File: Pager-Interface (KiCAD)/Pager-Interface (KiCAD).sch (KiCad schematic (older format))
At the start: 18 parts

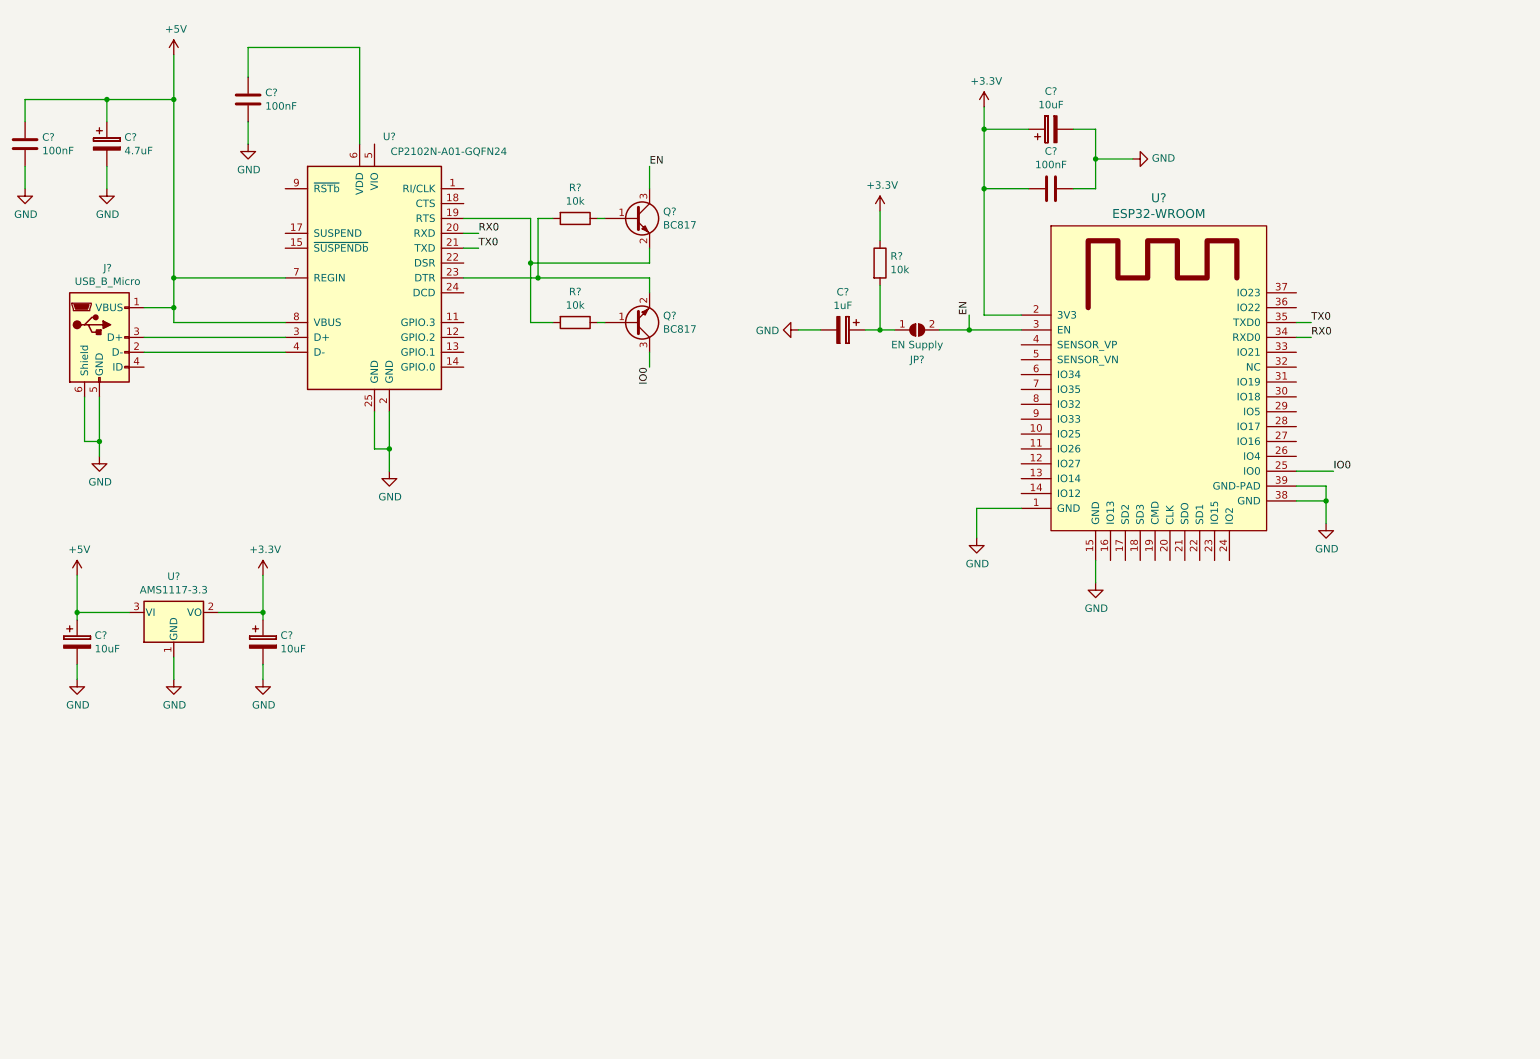
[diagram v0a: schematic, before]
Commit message: added si4432 symbol + added and connected si4432 in schematic
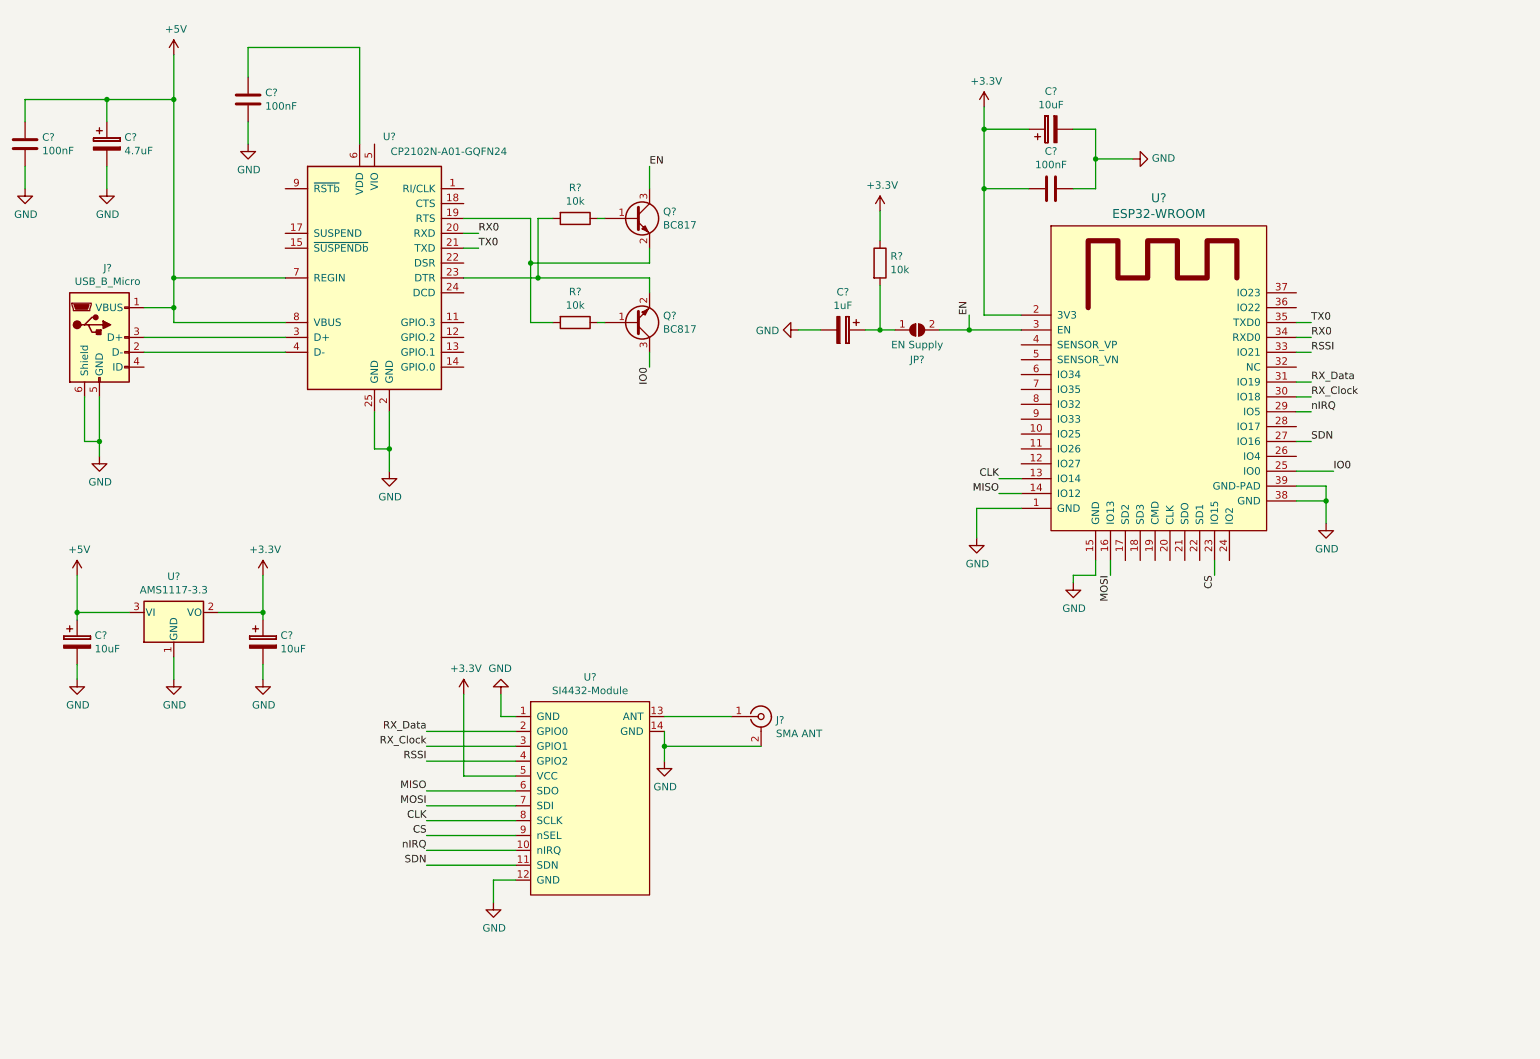
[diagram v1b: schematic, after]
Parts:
- added J?: SMA ANT, symbol Connector:Conn_Coaxial
- added U?: SI4432-Module, symbol si4432:SI4432-Module
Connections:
- net +3V3: now also U?.5 (VCC)
- net GND: now also J?.2 (Ext), U?.1 (GND), U?.12 (GND), U?.14 (GND)
- net CLK: now reaches U?.13 (IO14)
- net CLK: now also U?.8 (SCLK)
- net MISO: now reaches U?.14 (IO12)
- net MISO: now also U?.6 (SDO)
- net MOSI: now reaches U?.16 (IO13)
- net MOSI: now also U?.7 (SDI)
- net CS: now reaches U?.23 (IO15)
- net CS: now also U?.9 (nSEL)
- net SDN: now reaches U?.27 (IO16)
- net SDN: now also U?.11 (SDN)
- net nIRQ: now reaches U?.29 (IO5)
- net nIRQ: now also U?.10 (nIRQ)
- net RX_Clock: now reaches U?.30 (IO18)
- net RX_Clock: now also U?.3 (GPIO1)
- net RX_Data: now reaches U?.31 (IO19)
- net RX_Data: now also U?.2 (GPIO0)
- net RSSI: now reaches U?.33 (IO21)
- net RSSI: now also U?.4 (GPIO2)
- new net: J?.1 (In), U?.13 (ANT)
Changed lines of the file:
@@
 L power:GND #PWR?
 U 1 1 6037F357
-P 8150 4500
-F 0 "#PWR?" H 8150 4250 50  0001 C CNN
-F 1 "GND" H 8155 4327 50  0000 C CNN
-F 2 "" H 8150 4500 50  0001 C CNN
-F 3 "" H 8150 4500 50  0001 C CNN
-	1    8150 4500
-	1    0    0    -1
-$EndComp
-Wire Wire Line
-	8150 4350 8150 4500
+P 8000 4500
+F 0 "#PWR?" H 8000 4250 50  0001 C CNN
+F 1 "GND" H 8005 4327 50  0000 C CNN
+F 2 "" H 8000 4500 50  0001 C CNN
+F 3 "" H 8000 4500 50  0001 C CNN
+	1    8000 4500
+	1    0    0    -1
+$EndComp
 Wire Wire Line
 	9500 3850 9700 3850
@@
 	2550 4450 2550 4700
 Connection ~ 2550 4700
+$Comp
+L si4432:SI4432-Module U?
+U 1 1 6039ABF6
+P 4750 5900
+F 0 "U?" H 4750 6665 50  0000 C CNN
+F 1 "SI4432-Module" H 4750 6574 50  0000 C CNN
+F 2 "" H 5400 6450 50  0001 C CNN
+F 3 "" H 5400 6450 50  0001 C CNN
+	1    4750 5900
+	1    0    0    -1
+$EndComp
+$Comp
+L Connector:Conn_Coaxial J?
+U 1 1 6039ADF5
+P 5900 5400
+F 0 "J?" H 6000 5376 50  0000 L CNN
+F 1 "SMA ANT" H 6000 5285 50  0000 L CNN
+F 2 "" H 5900 5400 50  0001 C CNN
+F 3 " ~" H 5900 5400 50  0001 C CNN
+	1    5900 5400
+	1    0    0    -1
+$EndComp
+Wire Wire Line
+	5250 5400 5700 5400
+Wire Wire Line
+	5900 5600 5250 5600
+Wire Wire Line
+	5250 5600 5250 5500
+Wire Wire Line
+	4250 5400 4150 5400
+Wire Wire Line
+	4150 5400 4150 5250
+Wire Wire Line
+	4250 6500 4100 6500
+Wire Wire Line
+	4100 6500 4100 6650
+$Comp
+L power:GND #PWR?
+U 1 1 603A1EF6
+P 5250 5700
+F 0 "#PWR?" H 5250 5450 50  0001 C CNN
+F 1 "GND" H 5255 5527 50  0000 C CNN
+F 2 "" H 5250 5700 50  0001 C CNN
+F 3 "" H 5250 5700 50  0001 C CNN
+	1    5250 5700
+	1    0    0    -1
+$EndComp
+Wire Wire Line
+	5250 5600 5250 5700
+Connection ~ 5250 5600
+$Comp
+L power:GND #PWR?
+U 1 1 603A3E00
+P 4150 5250
+F 0 "#PWR?" H 4150 5000 50  0001 C CNN
+F 1 "GND" H 4155 5077 50  0000 C CNN
+F 2 "" H 4150 5250 50  0001 C CNN
+F 3 "" H 4150 5250 50  0001 C CNN
+	1    4150 5250
+	-1   0    0    1
+$EndComp
+$Comp
+L power:GND #PWR?
+U 1 1 603A3EA1
+P 4100 6650
+F 0 "#PWR?" H 4100 6400 50  0001 C CNN
+F 1 "GND" H 4105 6477 50  0000 C CNN
+F 2 "" H 4100 6650 50  0001 C CNN
+F 3 "" H 4100 6650 50  0001 C CNN
+	1    4100 6650
+	1    0    0    -1
+$EndComp
+Wire Wire Line
+	4250 5800 3900 5800
+Wire Wire Line
+	3900 5800 3900 5250
+$Comp
+L power:+3.3V #PWR?
+U 1 1 603A5FDC
+P 3900 5250
+F 0 "#PWR?" H 3900 5100 50  0001 C CNN
+F 1 "+3.3V" H 3915 5423 50  0000 C CNN
+F 2 "" H 3900 5250 50  0001 C CNN
+F 3 "" H 3900 5250 50  0001 C CNN
+	1    3900 5250
+	1    0    0    -1
+$EndComp
+Wire Wire Line
+	4250 5500 3650 5500
+Wire Wire Line
+	4250 5600 3650 5600
+Wire Wire Line
+	4250 5700 3650 5700
+Text Label 3650 5500 2    50   ~ 0
+RX_Data
+Text Label 3650 5600 2    50   ~ 0
+RX_Clock
+Text Label 3650 5700 2    50   ~ 0
+RSSI
+Wire Wire Line
+	4250 5900 3650 5900
+Wire Wire Line
+	4250 6000 3650 6000
+Wire Wire Line
+	4250 6100 3650 6100
+Wire Wire Line
+	4250 6200 3650 6200
+Text Label 3650 5900 2    50   ~ 0
+MISO
+Text Label 3650 6000 2    50   ~ 0
+MOSI
+Text Label 3650 6100 2    50   ~ 0
+CLK
+Text Label 3650 6200 2    50   ~ 0
+CS
+Wire Wire Line
+	4250 6300 3650 6300
+Wire Wire Line
+	4250 6400 3650 6400
+Text Label 3650 6300 2    50   ~ 0
+nIRQ
+Text Label 3650 6400 2    50   ~ 0
+SDN
+Text Label 9600 3250 0    50   ~ 0
+RX_Clock
+Wire Wire Line
+	9500 3250 9600 3250
+Text Label 9600 3150 0    50   ~ 0
+RX_Data
+Wire Wire Line
+	9500 3150 9600 3150
+Text Label 9600 2950 0    50   ~ 0
+RSSI
+Wire Wire Line
+	9500 2950 9600 2950
+Text Label 9600 3350 0    50   ~ 0
+nIRQ
+Wire Wire Line
+	9600 3350 9500 3350
+Text Label 9600 3550 0    50   ~ 0
+SDN
+Wire Wire Line
+	9500 3550 9600 3550
+Text Label 7500 3900 2    50   ~ 0
+MISO
+Wire Wire Line
+	7650 3900 7500 3900
+Text Label 8250 4450 3    50   ~ 0
+MOSI
+Wire Wire Line
+	8150 4350 8150 4450
+Wire Wire Line
+	8150 4450 8000 4450
+Wire Wire Line
+	8000 4450 8000 4500
+Wire Wire Line
+	8250 4350 8250 4450
+Text Label 7500 3800 2    50   ~ 0
+CLK
+Wire Wire Line
+	7650 3800 7500 3800
+Text Label 8950 4450 3    50   ~ 0
+CS
+Wire Wire Line
+	8950 4350 8950 4450
 $EndSCHEMATC

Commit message: change caps
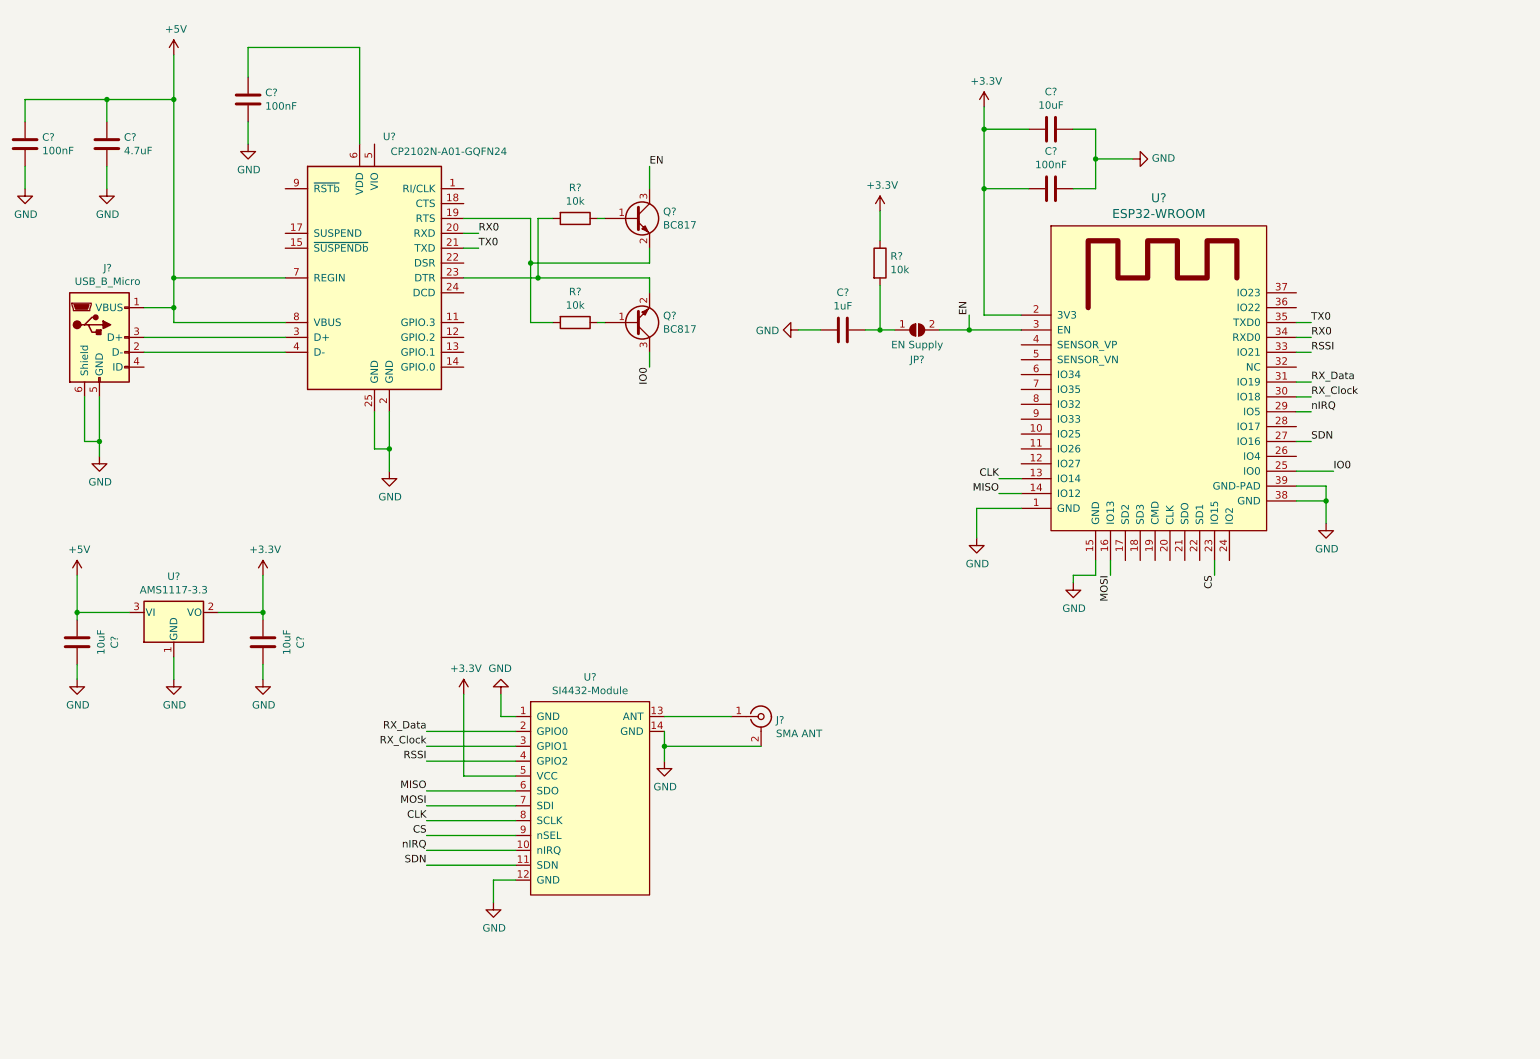
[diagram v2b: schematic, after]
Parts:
- removed C?: 4.7uF, symbol Device:CP
- removed C?: 1uF, symbol Device:CP
- removed C? (x3): 10uF, symbol Device:CP
- added C?: 1uF, symbol Device:C
- added C? (x3): 10uF, symbol Device:C
- added C?: 4.7uF, symbol Device:C
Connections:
- net +3V3: now also C?.2, C?.2
- net +5V: now also C?.2, C?.2
- net GND: now also C?.1, C?.1, C?.1, C?.1, C?.2
- net at JP?.1 (A), R?.2: now also C?.1
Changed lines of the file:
@@
-	1    0    0    -1
-$EndComp
-$Comp
-L Device:CP C?
-U 1 1 60367868
-P 1500 1550
-F 0 "C?" H 1618 1596 50  0000 L CNN
-F 1 "4.7uF" H 1618 1505 50  0000 L CNN
-F 2 "" H 1538 1400 50  0001 C CNN
-F 3 "~" H 1500 1550 50  0001 C CNN
-	1    1500 1550
 	1    0    0    -1
 $EndComp
@@
 	6150 2800 6300 2800
 $Comp
-L Device:CP C?
-U 1 1 603756E1
-P 6450 2800
-F 0 "C?" V 6195 2800 50  0000 C CNN
-F 1 "1uF" V 6286 2800 50  0000 C CNN
-F 2 "" H 6488 2650 50  0001 C CNN
-F 3 "~" H 6450 2800 50  0001 C CNN
-	1    6450 2800
-	0    1    1    0
-$EndComp
-$Comp
 L Device:R R?
 U 1 1 6037582E
@@
 	1    7400 1300
 	1    0    0    -1
-$EndComp
-$Comp
-L Device:CP C?
-U 1 1 60377FF9
-P 7850 1450
-F 0 "C?" V 8105 1450 50  0000 C CNN
-F 1 "10uF" V 8014 1450 50  0000 C CNN
-F 2 "" H 7888 1300 50  0001 C CNN
-F 3 "~" H 7850 1450 50  0001 C CNN
-	1    7850 1450
-	0    -1   -1   0
 $EndComp
 $Comp
@@
 	1    0    0    -1
 $EndComp
-$Comp
-L Device:CP C?
-U 1 1 603895A4
-P 1300 4900
-F 0 "C?" H 1418 4946 50  0000 L CNN
-F 1 "10uF" H 1418 4855 50  0000 L CNN
-F 2 "" H 1338 4750 50  0001 C CNN
-F 3 "~" H 1300 4900 50  0001 C CNN
-	1    1300 4900
-	1    0    0    -1
-$EndComp
-$Comp
-L Device:CP C?
-U 1 1 603895FE
-P 2550 4900
-F 0 "C?" H 2668 4946 50  0000 L CNN
-F 1 "10uF" H 2668 4855 50  0000 L CNN
-F 2 "" H 2588 4750 50  0001 C CNN
-F 3 "~" H 2550 4900 50  0001 C CNN
-	1    2550 4900
-	1    0    0    -1
-$EndComp
 Wire Wire Line
 	1300 4750 1300 4700
@@
 Wire Wire Line
 	8950 4350 8950 4450
+$Comp
+L Device:C C?
+U 1 1 603E1A86
+P 6450 2800
+F 0 "C?" V 6198 2800 50  0000 C CNN
+F 1 "1uF" V 6289 2800 50  0000 C CNN
+F 2 "" H 6488 2650 50  0001 C CNN
+F 3 "~" H 6450 2800 50  0001 C CNN
+	1    6450 2800
+	0    1    1    0
+$EndComp
+$Comp
+L Device:C C?
+U 1 1 603E1C23
+P 7850 1450
+F 0 "C?" V 7598 1450 50  0000 C CNN
+F 1 "10uF" V 7689 1450 50  0000 C CNN
+F 2 "" H 7888 1300 50  0001 C CNN
+F 3 "~" H 7850 1450 50  0001 C CNN
+	1    7850 1450
+	0    1    1    0
+$EndComp
+$Comp
+L Device:C C?
+U 1 1 603E1E7F
+P 1300 4900
+F 0 "C?" V 1048 4900 50  0000 C CNN
+F 1 "10uF" V 1139 4900 50  0000 C CNN
+F 2 "" H 1338 4750 50  0001 C CNN
+F 3 "~" H 1300 4900 50  0001 C CNN
+	1    1300 4900
+	-1   0    0    1
+$EndComp
+$Comp
+L Device:C C?
+U 1 1 603E20BD
+P 2550 4900
+F 0 "C?" V 2298 4900 50  0000 C CNN
+F 1 "10uF" V 2389 4900 50  0000 C CNN
+F 2 "" H 2588 4750 50  0001 C CNN
+F 3 "~" H 2550 4900 50  0001 C CNN
+	1    2550 4900
+	-1   0    0    1
+$EndComp
+$Comp
+L Device:C C?
+U 1 1 603E22DF
+P 1500 1550
+F 0 "C?" H 1385 1504 50  0000 R CNN
+F 1 "4.7uF" H 1385 1595 50  0000 R CNN
+F 2 "" H 1538 1400 50  0001 C CNN
+F 3 "~" H 1500 1550 50  0001 C CNN
+	1    1500 1550
+	-1   0    0    1
+$EndComp
 $EndSCHEMATC

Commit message: assigned footprints v2
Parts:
- C1, C2, C3, C4, C5, C6, C7, C8: renamed from C?; footprint (none) -> Capacitor_SMD:C_0805_2012Metric_Pad1.15x1.40mm_HandSolder
- J1: renamed from J?; footprint (none) -> Connector_USB:USB_Micro-B_GCT_USB3076-30-A; JCLC (none) -> https://lcsc.com/product-detail/USB-Connectors_Shenzhen-Kin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
- J2: renamed from J?; footprint (none) -> Connector_Coaxial:SMA_Amphenol_132289_EdgeMount; JCLC (none) -> https://lcsc.com/product-detail/RF-Connectors-Coaxial-Conne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
- JP1: renamed from JP?; footprint (none) -> Jumper:SolderJumper-2_P1.3mm_Open_Pad1.0x1.5mm
- R1, R2, R3: renamed from R?; footprint (none) -> Resistor_SMD:R_0805_2012Metric_Pad1.15x1.40mm_HandSolder
- gave numbers to parts that had none: 6

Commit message: added footprint for si4432 module + created pcb
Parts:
- U3: footprint (none) -> SI4432 Module:SI4432-Module
- U4: footprint ESP32-footprints-Lib:ESP32-WROOM -> ESP32:ESP32-WROOM
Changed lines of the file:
@@
 F 0 "U4" H 8575 4687 60  0000 C CNN
 F 1 "ESP32-WROOM" H 8575 4581 60  0000 C CNN
-F 2 "ESP32-footprints-Lib:ESP32-WROOM" H 8950 4650 60  0001 C CNN
+F 2 "ESP32:ESP32-WROOM" H 8950 4650 60  0001 C CNN
 F 3 "" H 8150 3750 60  0001 C CNN
 	1    8600 3300
@@
 F 0 "U3" H 4750 6665 50  0000 C CNN
 F 1 "SI4432-Module" H 4750 6574 50  0000 C CNN
-F 2 "" H 5400 6450 50  0001 C CNN
+F 2 "SI4432 Module:SI4432-Module" H 5400 6450 50  0001 C CNN
 F 3 "" H 5400 6450 50  0001 C CNN
 	1    4750 5900
